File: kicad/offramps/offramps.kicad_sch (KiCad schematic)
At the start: 225 parts, among them J10 Conn_01x04_Socket, J11 Screw_Terminal_01x02, J12 Conn_01x04_Pin, J13 Micro_SD_Card_Det1, J14 Conn_01x03_Male, J15 Screw_Terminal_01x02, J16 Conn_01x02_Pin, J17 Conn_01x02_Pin, J3 VITA_57.1_FMC_HPC_Carrier, J4 Conn_01x02_Pin, J5 Conn_Coaxial, J6 Conn_01x03_Male, J7 Conn_Coaxial, J8 Conn_Coaxial, J9 Conn_01x06_Male, Q1 BSS138, Q10 BSS138, Q11 BSS138, Q12 BSS138, Q13 NPN, Q14 NPN, Q15 NPN, Q16 NPN, Q17 BSS138, Q18 BSS138, Q19 NPN, Q2 BSS138, Q25 BSS138, Q26 BSS138, Q27 BSS138, Q28 BSS138, Q29 BSS138, Q3 BSS138, Q30 BSS138, Q4 BSS138, Q5 BSS138, Q6 BSS138, Q7 BSS138, Q8 BSS138, Q9 BSS138, SW1 219-8MSTR, U1 TXB0108PWR, U10 MCP4725xxx-xCH, U11 LMH6611MK/NOPB, U12 ADC1173CIMTCX/NOPB, U13 MCP4725xxx-xCH, U14 OPA2994IDGKR, U15 ADS1114IDGSR, U16 LIS2MDLTR, U17 LSM6DSRTR, U18 LTC-4627JR, U19 AMS1117-3.3, U2 TXB0108PWR, U20 LM358DR2G, U3 TXB0108PWR, U4 TXB0108PWR, U5 TXB0108PWR, U6 LMH6611MK/NOPB, U7 ADC1175-50CIMTCX/NOPB, U8 TXB0108PWR, U9 PTMUX4053PWR

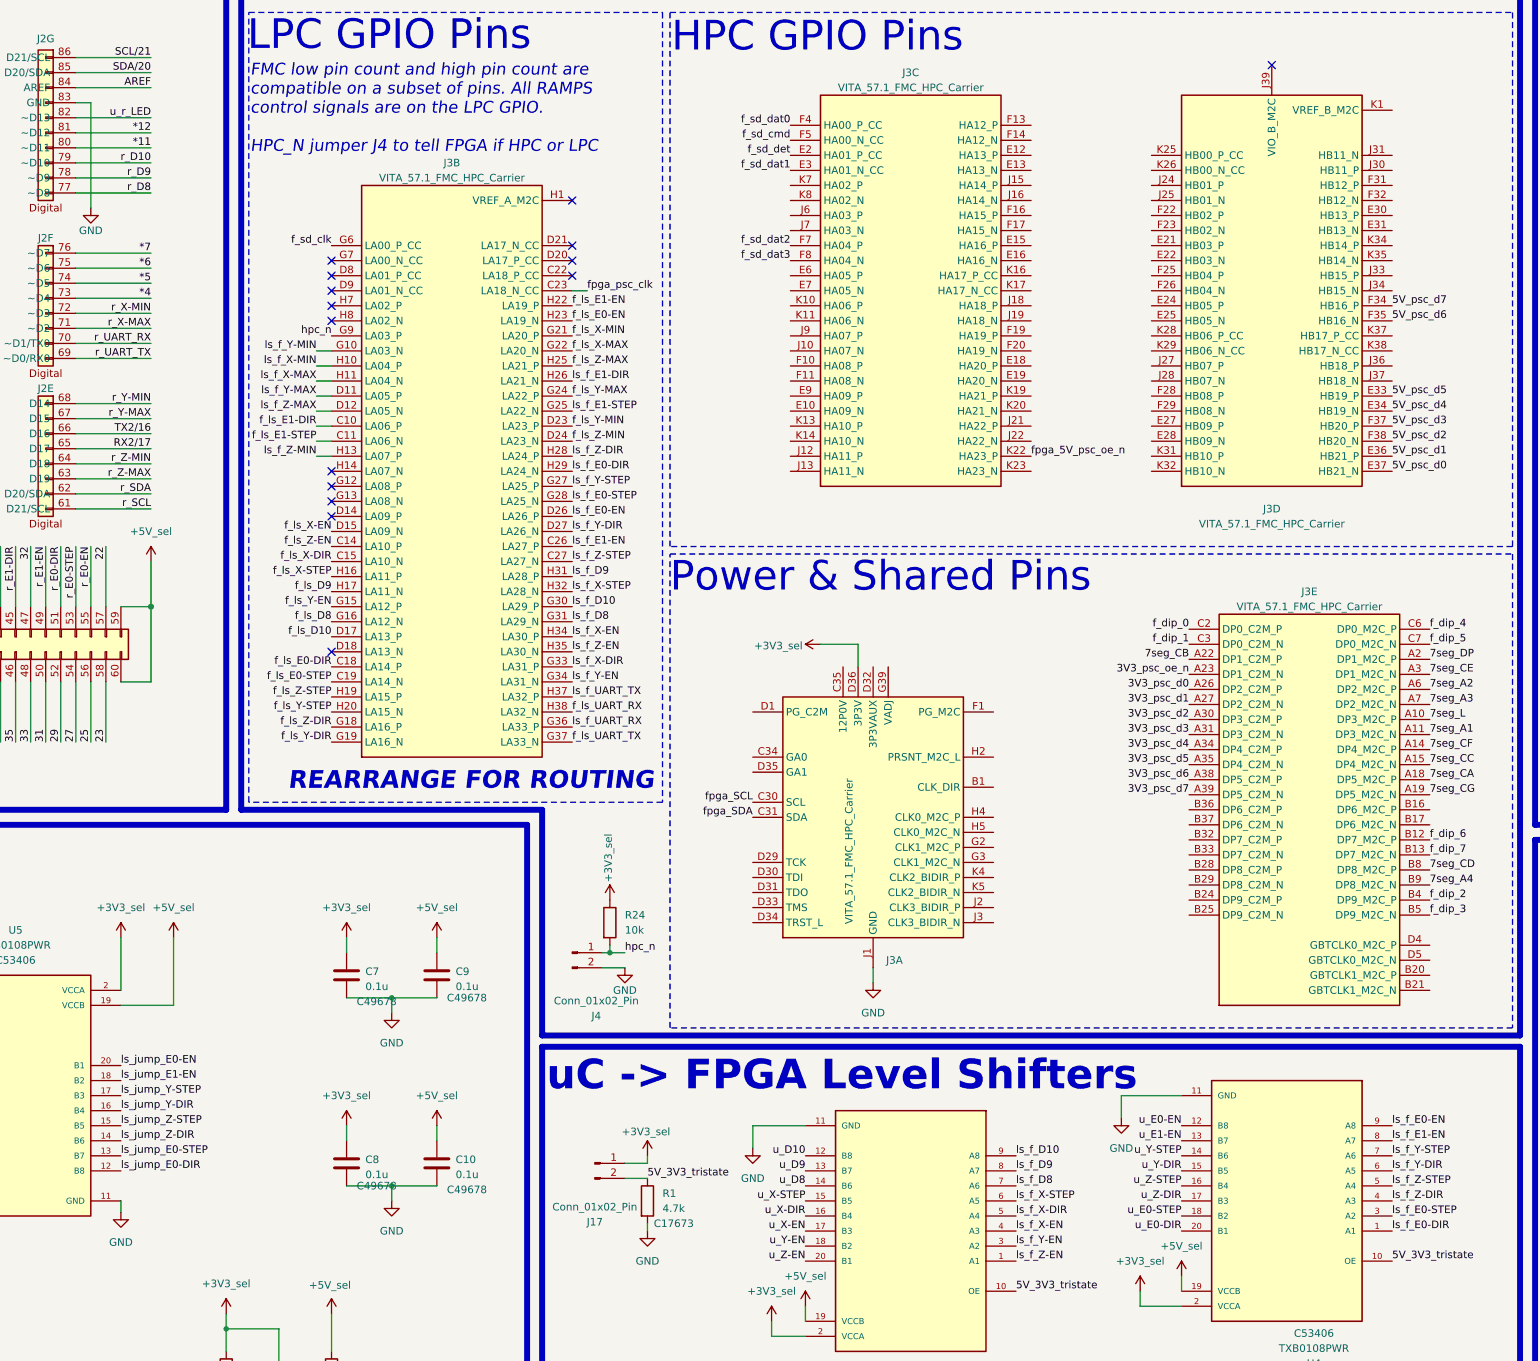
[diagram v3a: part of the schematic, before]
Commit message: Fixed NC flags on FMC.
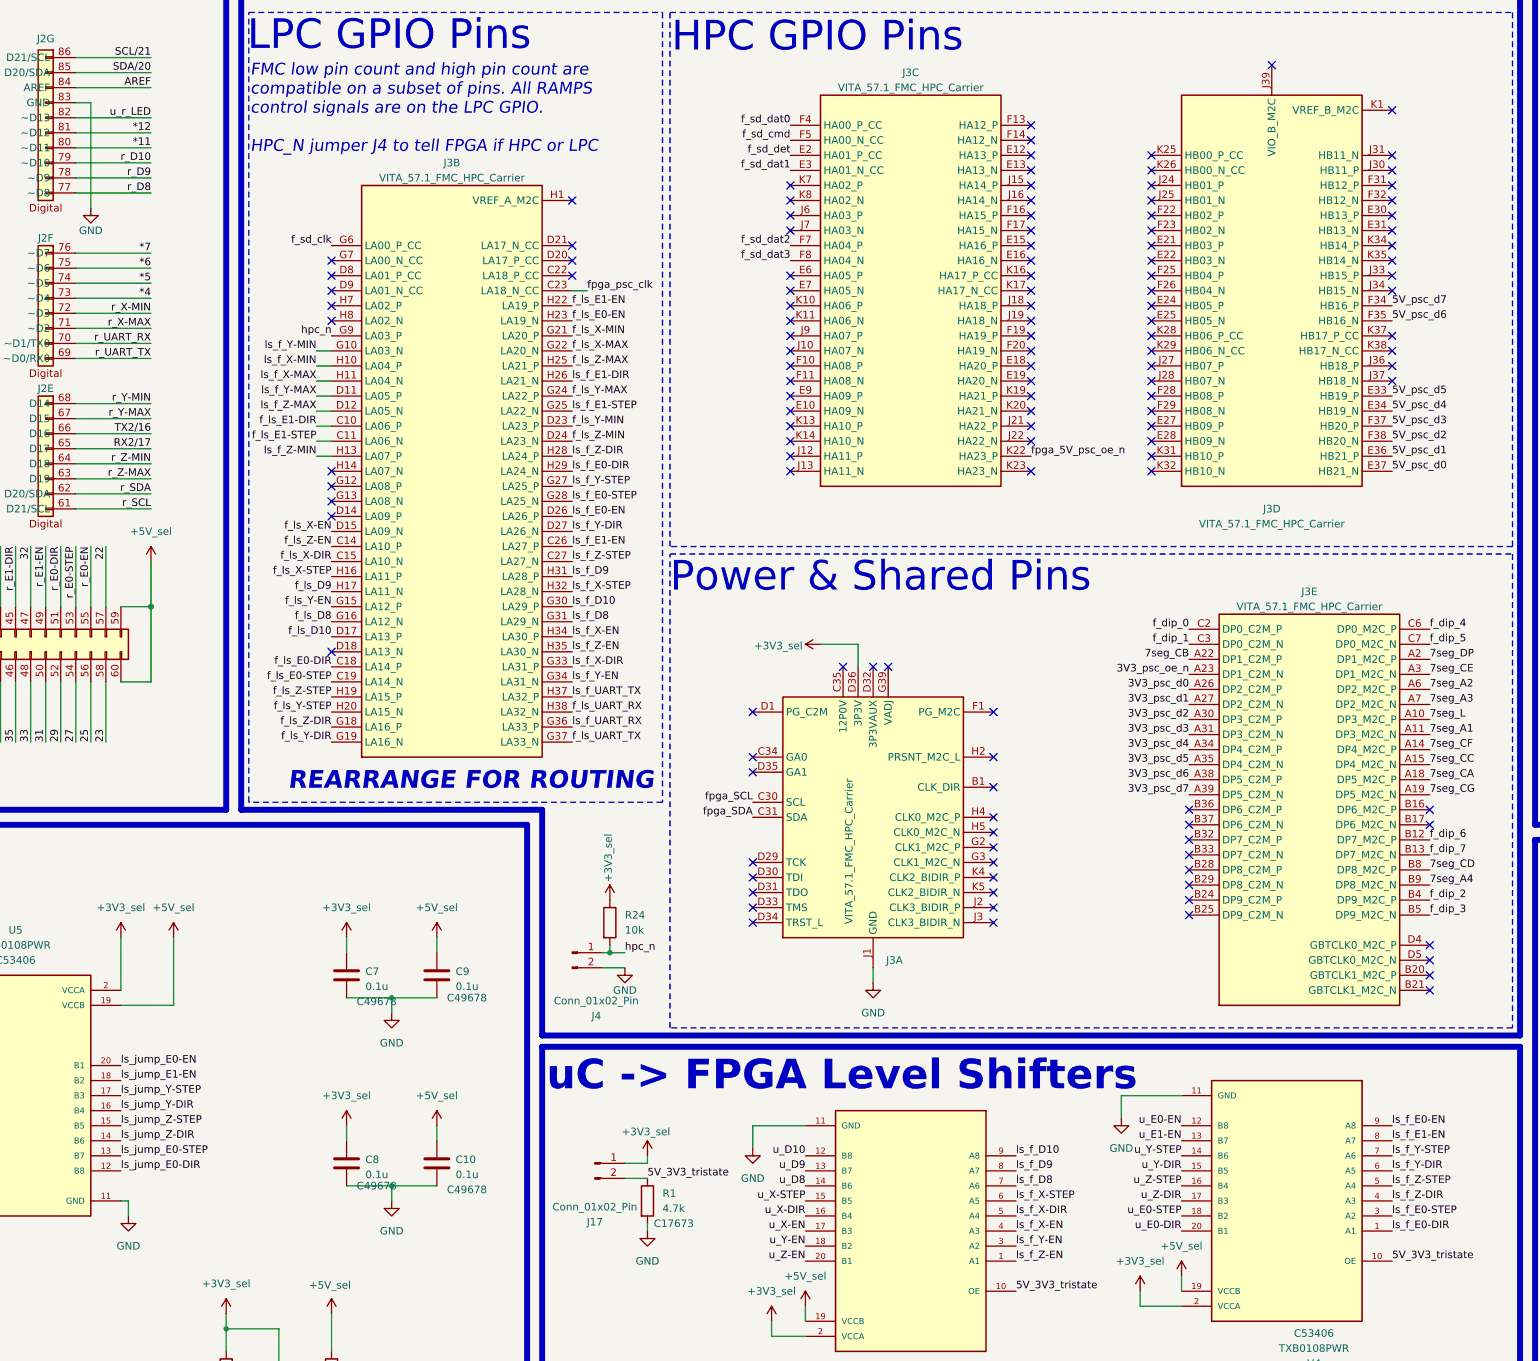
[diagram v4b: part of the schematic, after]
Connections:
- no-connect marks 24 -> 138

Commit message: General updates
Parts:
- removed Q1, Q2, Q3, Q4, Q5, Q6: BSS138, Package_TO_SOT_SMD:SOT-23, symbol Transistor_FET:BSS138
- removed R2, R3, R5, R6, R8, R9: 10k, Resistor_SMD:R_0805_2012Metric, symbol Device:R
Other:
- note removed: "CHECK THIS http://ww1.microchip.com/downloads/en/DeviceDoc/chapter%208.pdf"
- note removed: "CW Nano schematic and documentation reference have notable differences..."
- note removed: "Orignal Design: (Excluded from board)"
- note removed: "Power Analysis Test Points"
- note removed: "REARRANGE FOR ROUTING"
- note removed: "Shift to 5V Needs to be low latency"
- note removed: "Swap for 10 resistor chip"
- note removed: "VGND?"
- note removed: "to be added as needed"
- company: (none) -> New York University
- title: (none) -> OffRAMPS
- moved on the sheet: C12, C14, C15, C16, C17, C18, C19, C20, C22, C25, C26, C27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
